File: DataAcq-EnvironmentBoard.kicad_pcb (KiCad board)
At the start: 2 copper layers, 45.8 x 50.2 mm, 23 parts, among them J2 CAN Output, J3 CAN Input, U1 SHT45, U2 FS3000-1005, U3 LMT87DCK, U4 Daughterboard Connector

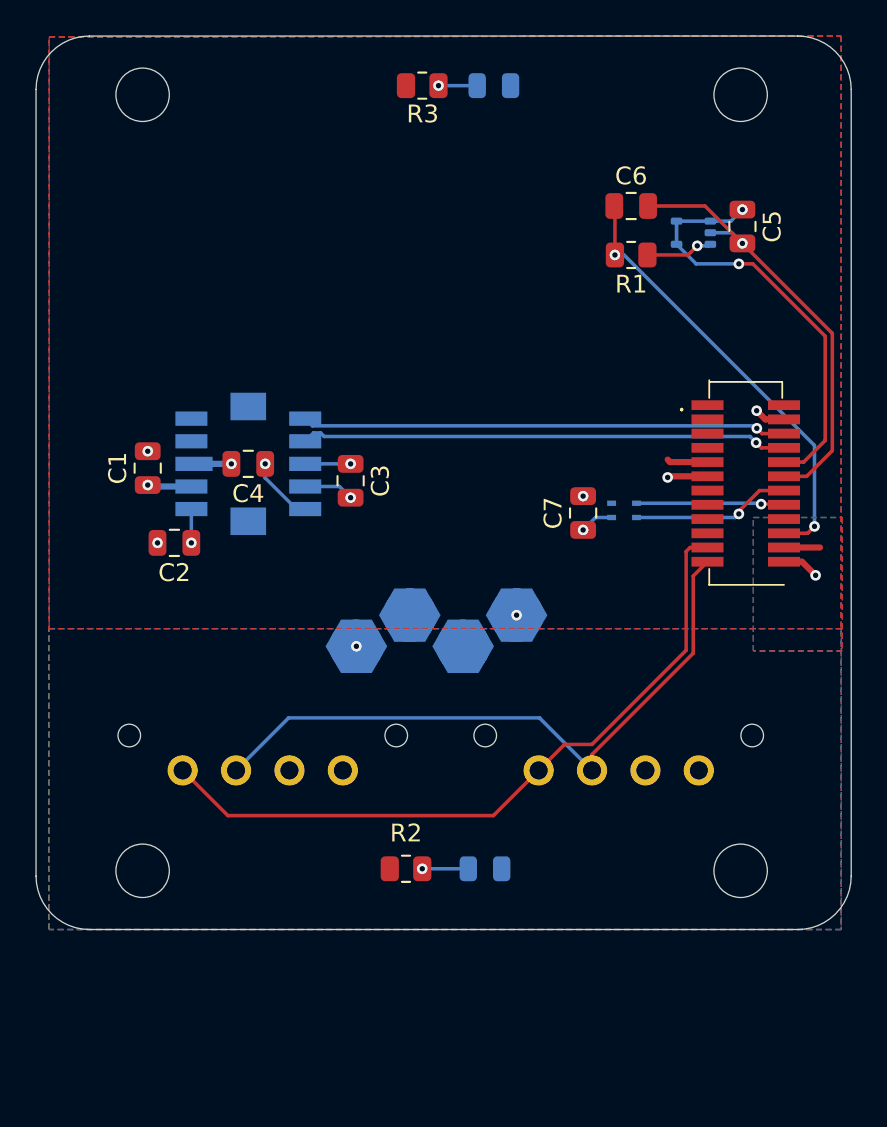
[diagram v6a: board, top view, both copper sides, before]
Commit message: add test point and redo CAN connections
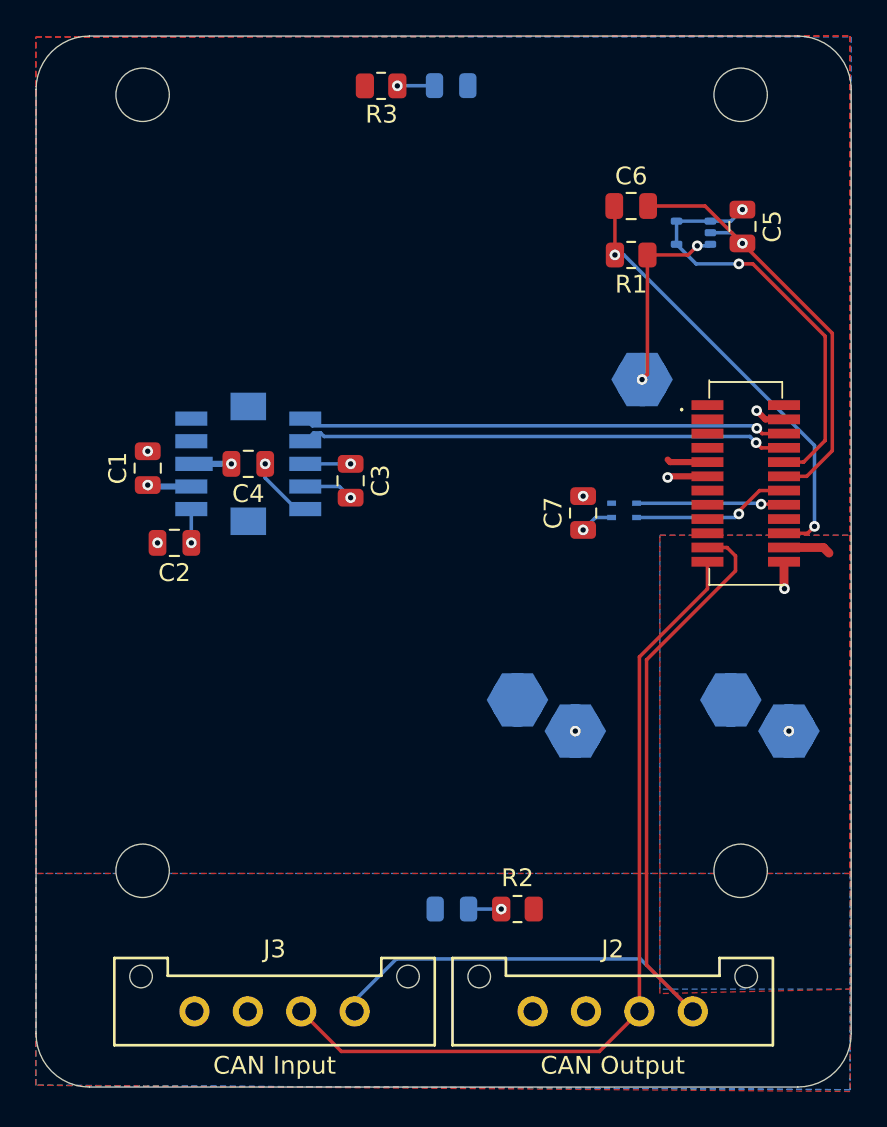
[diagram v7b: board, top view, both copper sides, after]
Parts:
- added TP3: TestPoint, UTSVT_Special:TestPoint_HEX_3mmID, B.Cu at (174.0, 90.5)
- J2, J3: moved to F.Cu
- moved J3 31.4 mm to (148.8, 126.0), turned to 0 degrees
- moved TP1 24.8 mm to (182.2, 110.2)
- moved J2 17.2 mm to (167.8, 126.0), turned to 0 degrees
- moved TP2 15.3 mm to (179.0, 108.5)
- moved TP5 7.70 mm to (167.0, 108.5)
- moved TP4 7.30 mm to (170.2, 110.2), turned to 90 degrees
- moved R2 6.66 mm to (167.0, 120.2), turned to 180 degrees
- moved D1 2.93 mm to (163.3, 120.2), turned to 0 degrees
- moved D2 2.40 mm to (163.3, 74.0)
- moved R3 2.31 mm to (159.3, 74.0)
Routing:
- net /CAN_L: track 40.0 -> 52.3 mm
- net /CAN_H: track 36.9 -> 47.7 mm
- net /TEMP_OUT: track 3.79 -> 10.9 mm, vias 1 -> 2
- net Net-(D1-A): track 2.59 -> 1.84 mm
- net +12V_In: track 2.03 -> 2.65 mm
- net GNDPWR: track 2.09 -> 1.56 mm
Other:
- board size 45.8 x 50.2 mm -> 45.8 x 59 mm
- board text added: "Airflow"
- board text added: "Data Acq Environment Board v1.0 Ravi Shah 2024"
- board text added: "TEMP"
- board text removed: "Data Acq Environment Board Ravi Shah 2024"

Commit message: add images and cleanup
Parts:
- added LOGO2: Dr. Hallock, UTSVT_Special:Hallock_Image_Tiny, B.Cu at (160.0, 107.3)
- added LOGO3: UTSVT Logo, UTSVT_Special:UTSVT_Logo_Symbol, B.Cu at (162.8, 85.2)
- added LOGO4: Wolf, images:wolf, B.Cu at (148.5, 108.0)
- moved TP3 1.35 mm to (172.8, 90.0)
